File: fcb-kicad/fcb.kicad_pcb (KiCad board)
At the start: 4 copper layers, 45 x 45 mm, 92 parts, among them J1 Conn_ESC_4in1, J10 PH1X3, J11 PH1X3, J2 SWD, J3 Conn_Coaxial, J4 PH1X4, J5 USB_B_Micro, J6 PH1X3, J7 PH1X3, J8 PH1X4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

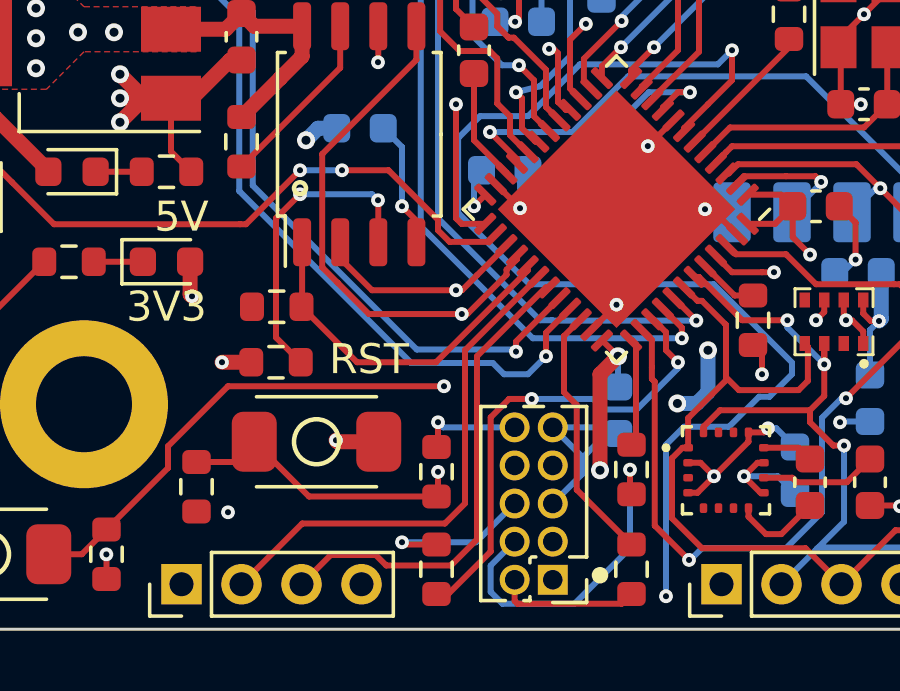
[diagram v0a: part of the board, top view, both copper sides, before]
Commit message: Change MCU to STM32F411CCU6
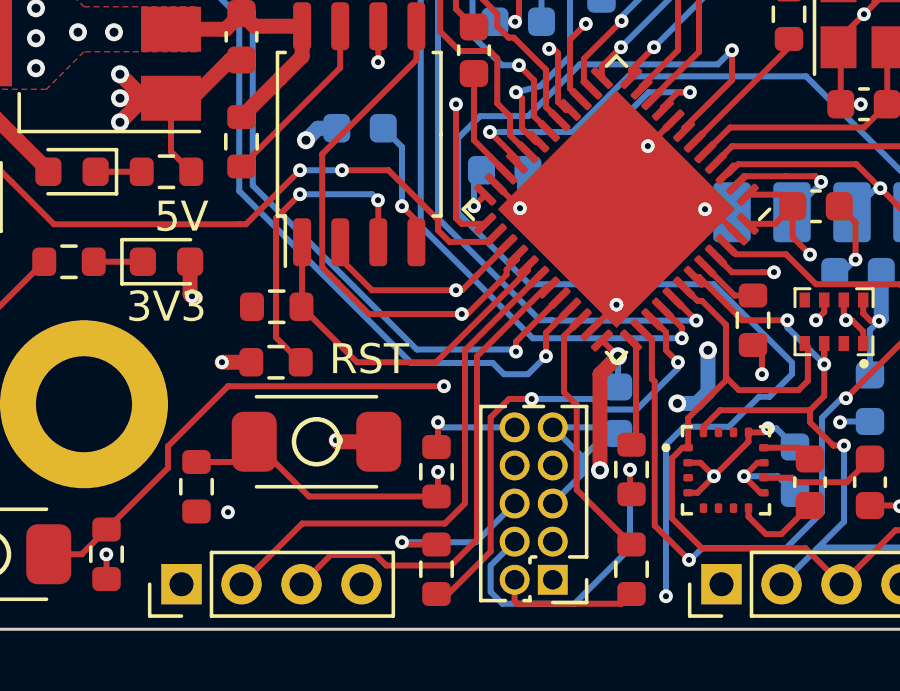
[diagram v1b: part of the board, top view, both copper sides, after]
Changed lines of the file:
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@@
     )
   )
-  (gr_circle (center 140.2 109.8) (end 140.4 109.8) (layer "F.SilkS") (width 0.15) (fill none))
-  (gr_circle (center 150.2 122.7) (end 150.4 122.7) (layer "F.SilkS") (width 0.15) (fill solid))
   (gr_circle (center 152 89.8) (end 152.2 89.8) (layer "F.SilkS") (width 0.15) (fill none))
   (gr_arc (start 127.5 124.5) (mid 126.085786 123.914214) (end 125.5 122.5) (layer "Edge.Cuts") (width 0.1))
